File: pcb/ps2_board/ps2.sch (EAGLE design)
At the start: 12 parts, among them IC3 STM32F042F4, J1 DIN7, J2 DIN7, SW4 324_SW

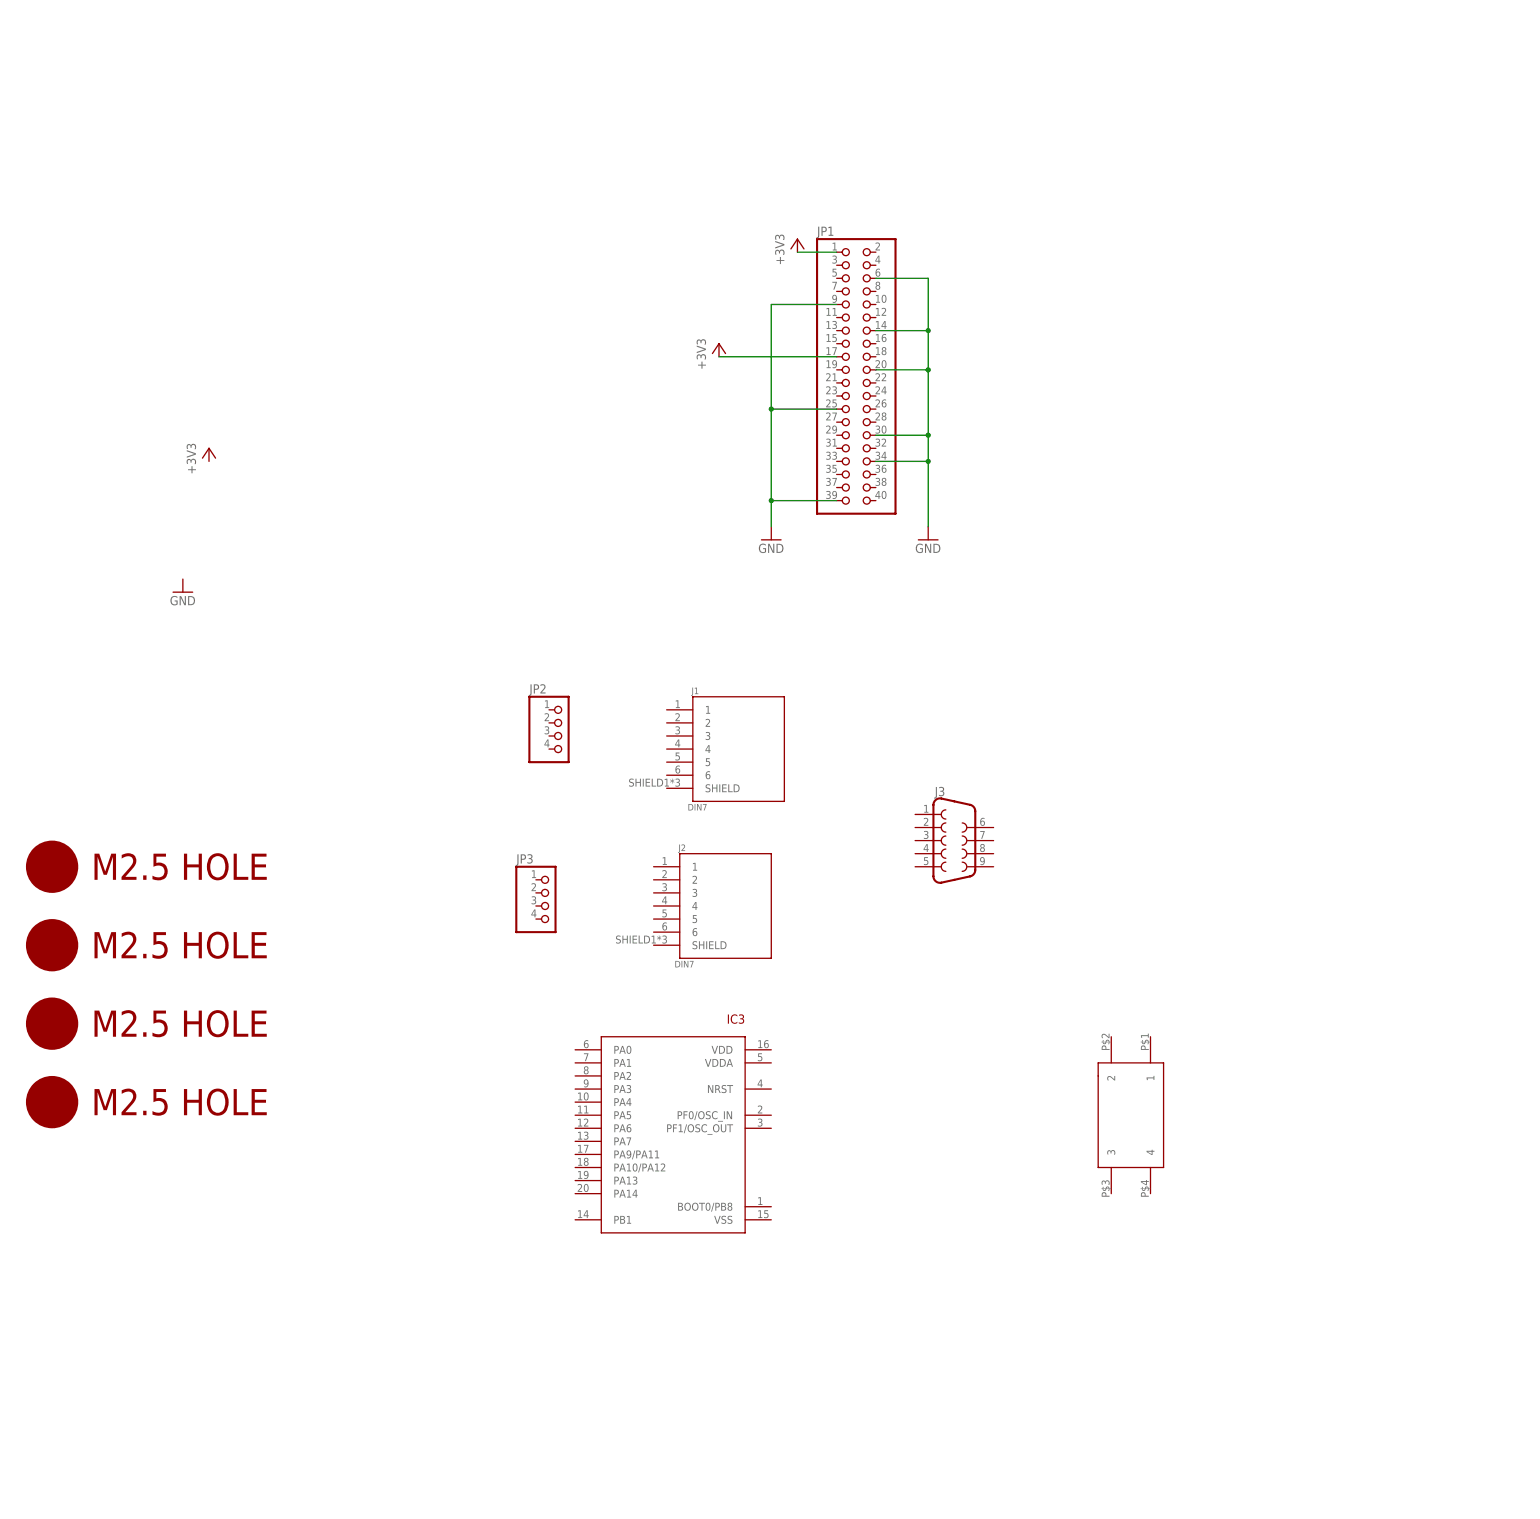
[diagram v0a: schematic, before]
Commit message: ps2 board done apart from max232
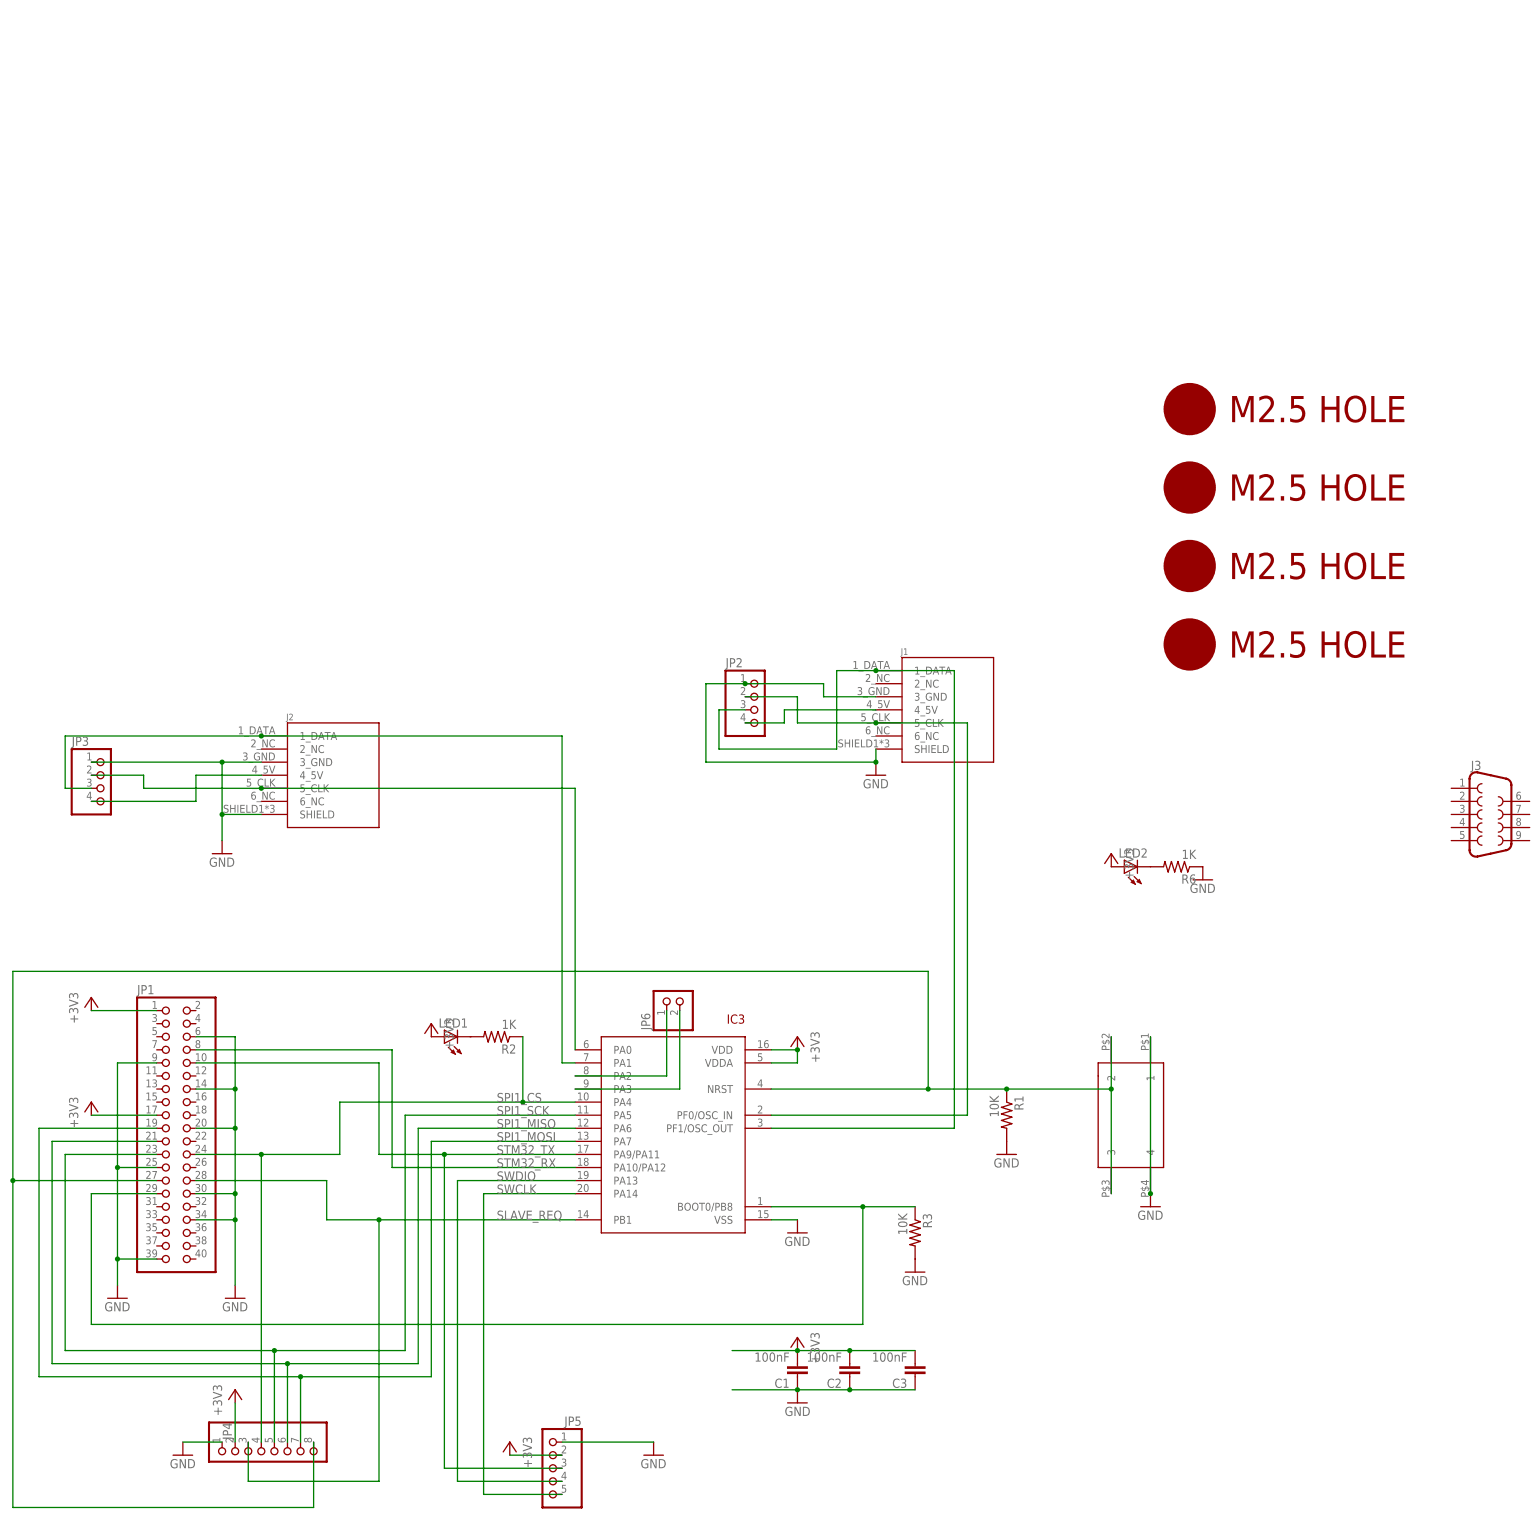
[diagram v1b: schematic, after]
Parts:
- added C1, C2, C3: 100nF, clock:CAP0805
- added JP4: (no value), pinhead:PINHD-1X8
- added JP5: (no value), pinhead:PINHD-1X5
- added JP6: (no value), pinhead:PINHD-1X2
- added LED1, LED2: (no value), adafruit:LEDCHIP-LED0805
- added R1, R3: 10K, SparkFun-Passives:RESISTOR0805-RES
- added R2, R6: 1K, SparkFun-Passives:RESISTOR0805-RES
- J1, J2: value DIN7 -> (none)
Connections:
- new net N$1: IC3.NRST, JP1.27, JP4.8, R1.1, SW4.2, SW4.3
- new net N$10: IC3.PA2, JP6.1
- new net N$11: IC3.PA3, JP6.2
- new net N$2: LED1.C, R2.2
- new net N$29: LED2.C, R6.2
- new net N$3: J1.4_5V, JP2.4
- new net N$4: J2.4_5V, JP3.4
- new net N$5: IC3.PF0/OSC_IN, J1.5_CLK, JP2.2
- new net N$6: IC3.PF1/OSC_OUT, J1.1_DATA, JP2.3
- new net N$7: IC3.PA0, J2.5_CLK, JP3.2
- new net N$8: IC3.PA1, J2.1_DATA, JP3.3
- new net N$9: IC3.BOOT0/PB8, JP1.29, R3.1
- new net SLAVE_REQ: IC3.PB1, JP1.28, JP4.3
- new net SPI1_CS: IC3.PA4, JP1.24, JP4.4, R2.1
- new net SPI1_MISO: IC3.PA6, JP1.21, JP4.6
- new net SPI1_MOSI: IC3.PA7, JP1.19, JP4.7
- new net SPI1_SCK: IC3.PA5, JP1.23, JP4.5
- new net STM32_RX: IC3.PA10/PA12, JP1.8
- new net STM32_TX: IC3.PA9/PA11, JP1.10, JP5.3
- new net SWCLK: IC3.PA14, JP5.5
- new net SWDIO: IC3.PA13, JP5.4
- net +3V3: now also C1.2, C2.2, C3.2, IC3.VDD, IC3.VDDA, JP4.2, JP5.2, LED1.A, LED2.A
- net GND: now also C1.1, C2.1, C3.1, IC3.VSS, J1.3_GND, J1.SHIELD, J2.3_GND, J2.SHIELD, JP2.1, JP3.1, JP4.1, JP5.1, R1.2, R3.2, R6.1, SW4.1, SW4.4
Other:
- moved on the sheet: J1, J2, J3, JP1, JP2, JP3

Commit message: ps2 board prototype done
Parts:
- added C4, C5, C6, C7, C9: 100nF, clock:CAP0805
- added JP10: (no value), pinhead:PINHD-2X4
- added JP11, JP7, JP8, JP9: (no value), pinhead:PINHD-1X4
- added U1: MAX3232, SparkFun-DigitalIC:MAX232SOIC16
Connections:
- new net C1+: C9.1, U1.C1+
- new net C1-: C9.2, U1.C1-
- new net C2+: C4.1, U1.C2+
- new net C2-: C4.2, U1.C2-
- new net N$12: JP8.1, U1.T2IN
- new net N$13: JP8.2, U1.R2OUT
- new net N$14: JP8.3, U1.T2OUT
- new net N$15: JP8.4, U1.R2IN
- new net N$16: J3.1, JP10.2
- new net N$17: J3.2, JP10.4
- new net N$18: J3.3, JP10.6
- new net N$19: J3.4, JP10.8
- new net N$20: J3.6, JP10.1
- new net N$21: J3.7, JP10.3
- new net N$22: J3.8, JP10.5
- new net N$23: J3.9, JP10.7
- new net RX1IN_232: JP7.2, U1.R1IN
- new net TX1OUT_232: JP7.1, U1.T1OUT
- new net V+: C6.1, U1.V+
- new net V-: C5.1, U1.V-
- net +3V3: now also C7.1, JP11.1, JP11.2, JP11.3, JP11.4, U1.VCC
- net GND: now also C5.2, C6.2, C7.2, J3.5, J3.SHIELD, JP9.1, JP9.2, JP9.3, JP9.4, U1.GND
- net STM32_RX: now also JP7.3, U1.R1OUT
- net STM32_TX: now also JP7.4, U1.T1IN
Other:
- note added: "3.0V < VCC < 5.5V"
- note added: "RS-232"
- note added: "TTL/CMOS"
- moved on the sheet: LED1, R2

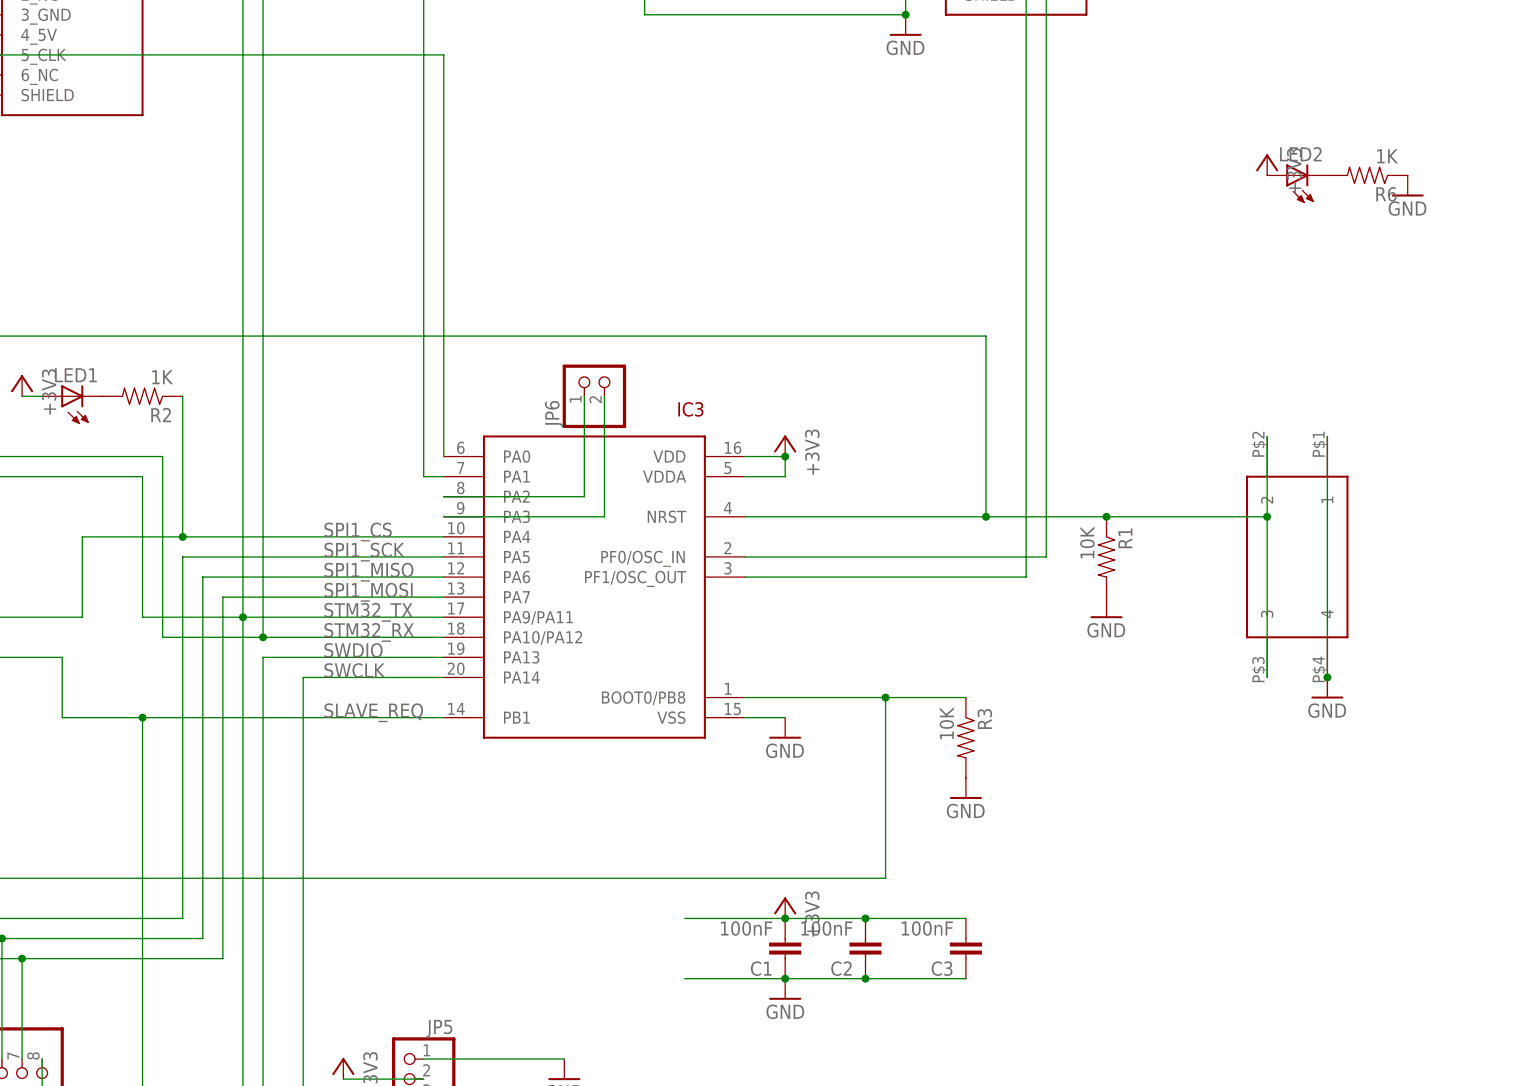
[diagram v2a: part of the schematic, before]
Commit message: double checked and adjusted resistor and cap values
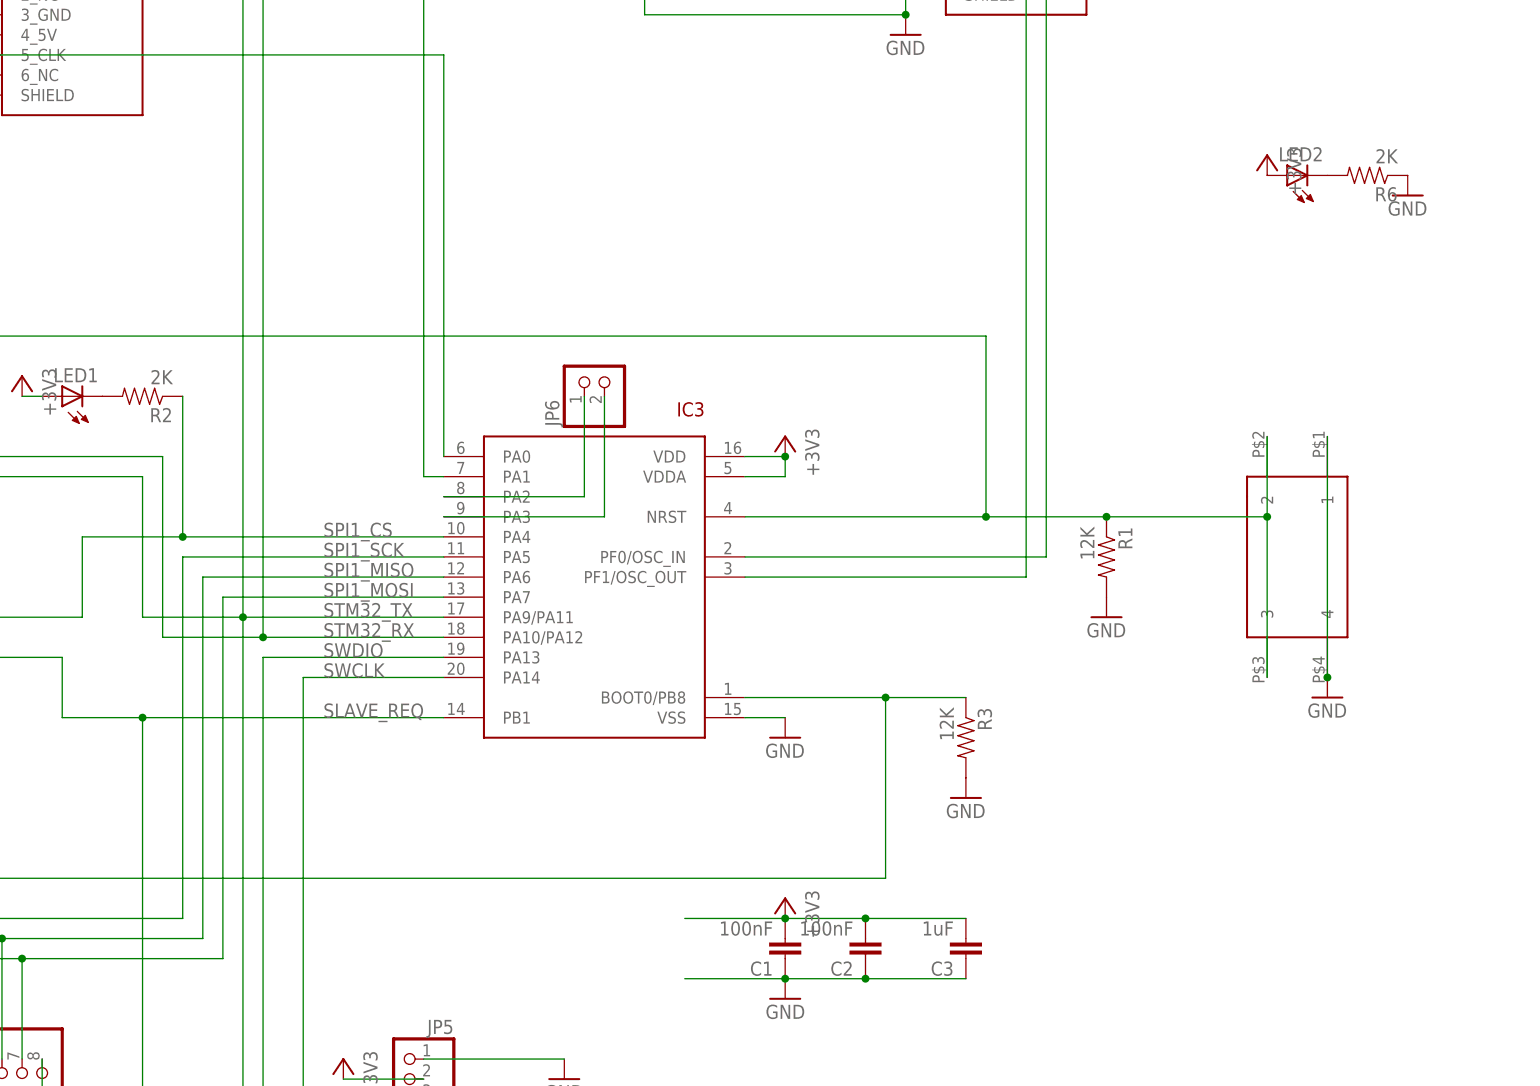
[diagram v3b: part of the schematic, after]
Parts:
- C3: value 100nF -> 1uF
- R1, R3: value 10K -> 12K
- R2, R6: value 1K -> 2K
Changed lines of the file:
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@@
 <part name="+3V16" library="backplane" deviceset="+3V3" device=""/>
 <part name="LED2" library="adafruit" deviceset="LED" device="CHIP-LED0805"/>
-<part name="R6" library="SparkFun-Passives" deviceset="RESISTOR" device="0805-RES" value="1K"/>
+<part name="R6" library="SparkFun-Passives" deviceset="RESISTOR" device="0805-RES" value="2K"/>
 <part name="GND9" library="backplane" deviceset="GND" device=""/>
 <part name="C1" library="clock" deviceset="CAP" device="0805" value="100nF"/>
 <part name="GND8" library="supply1" deviceset="GND" device=""/>
-<part name="R1" library="SparkFun-Passives" deviceset="RESISTOR" device="0805-RES" value="10K"/>
+<part name="R1" library="SparkFun-Passives" deviceset="RESISTOR" device="0805-RES" value="12K"/>
 <part name="GND4" library="supply1" library_urn="urn:adsk.eagle:library:371" deviceset="GND" device=""/>
 <part name="JP4" library="pinhead" library_urn="urn:adsk.eagle:library:325" deviceset="PINHD-1X8" device="" package3d_urn="urn:adsk.eagle:package:22409/2"/>
@@
 <part name="+3V4" library="supply1" library_urn="urn:adsk.eagle:library:371" deviceset="+3V3" device=""/>
 <part name="C2" library="clock" deviceset="CAP" device="0805" value="100nF"/>
-<part name="C3" library="clock" deviceset="CAP" device="0805" value="100nF"/>
+<part name="C3" library="clock" deviceset="CAP" device="0805" value="1uF"/>
 <part name="JP5" library="pinhead" library_urn="urn:adsk.eagle:library:325" deviceset="PINHD-1X5" device="" package3d_urn="urn:adsk.eagle:package:22469/2"/>
 <part name="GND6" library="supply1" library_urn="urn:adsk.eagle:library:371" deviceset="GND" device=""/>
@@
 <part name="+3V7" library="backplane" deviceset="+3V3" device=""/>
 <part name="LED1" library="adafruit" deviceset="LED" device="CHIP-LED0805"/>
-<part name="R2" library="SparkFun-Passives" deviceset="RESISTOR" device="0805-RES" value="1K"/>
-<part name="R3" library="SparkFun-Passives" deviceset="RESISTOR" device="0805-RES" value="10K"/>
+<part name="R2" library="SparkFun-Passives" deviceset="RESISTOR" device="0805-RES" value="2K"/>
+<part name="R3" library="SparkFun-Passives" deviceset="RESISTOR" device="0805-RES" value="12K"/>
 <part name="GND11" library="supply1" library_urn="urn:adsk.eagle:library:371" deviceset="GND" device=""/>
 <part name="JP6" library="pinhead" library_urn="urn:adsk.eagle:library:325" deviceset="PINHD-1X2" device="" package3d_urn="urn:adsk.eagle:package:22435/2"/>
